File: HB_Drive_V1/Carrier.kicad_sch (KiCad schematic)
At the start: 0 parts

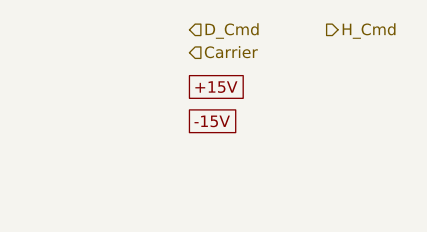
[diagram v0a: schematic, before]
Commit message: fixes git and adds a first revision of the Inner Current Regulator (NOT COMPLETE)
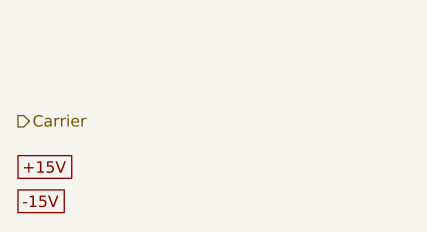
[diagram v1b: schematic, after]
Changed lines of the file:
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@@
 	(generator_version "10.0")
 	(paper "A4")
-	(global_label "-15V"
+	(global_label "+15V"
 		(shape passive)
-		(at 139.7 86.36 0)
+		(at 120.65 91.44 0)
 		(fields_autoplaced yes)
 		(effects
@@
 		)
 		(property "Intersheetrefs" "${INTERSHEET_REFS}"
-			(at 146.6539 86.36 0)
+			(at 127.6039 91.44 0)
 			(hide yes)
 			(show_name no)
@@
 		)
 	)
-	(global_label "+15V"
+	(global_label "-15V"
 		(shape passive)
-		(at 139.7 82.55 0)
+		(at 120.65 95.25 0)
 		(fields_autoplaced yes)
 		(effects
@@
 		)
 		(property "Intersheetrefs" "${INTERSHEET_REFS}"
-			(at 146.6539 82.55 0)
+			(at 127.6039 95.25 0)
 			(hide yes)
 			(show_name no)
@@
 		)
 	)
-	(hierarchical_label "D_Cmd"
-		(shape input)
-		(at 139.7 76.2 0)
+	(hierarchical_label "Carrier"
+		(shape output)
+		(at 120.65 86.36 0)
 		(effects
 			(font
-				(size 1.27 1.27)
-			)
-			(justify left)
-		)
-	)
-	(hierarchical_label "Carrier"
-		(shape input)
-		(at 139.7 78.74 0)
-		(effects
-			(font
-				(size 1.27 1.27)
-			)
-			(justify left)
-		)
-	)
-	(hierarchical_label "H_Cmd"
-		(shape output)
-		(at 154.94 76.2 0)
-		(effects
-			(font

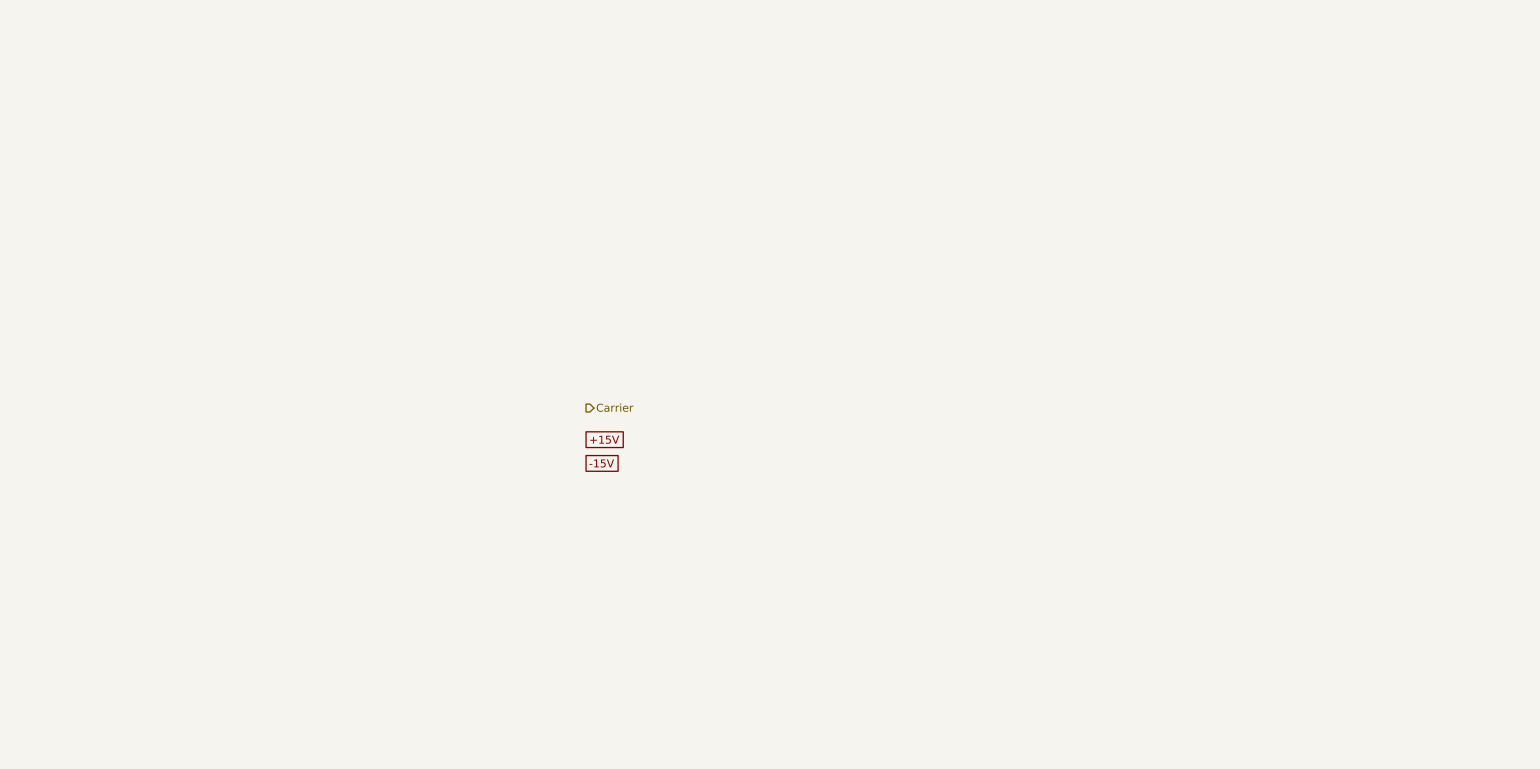
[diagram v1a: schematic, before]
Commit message: Adds Carrier Wave Circuit and Comparator Circuit
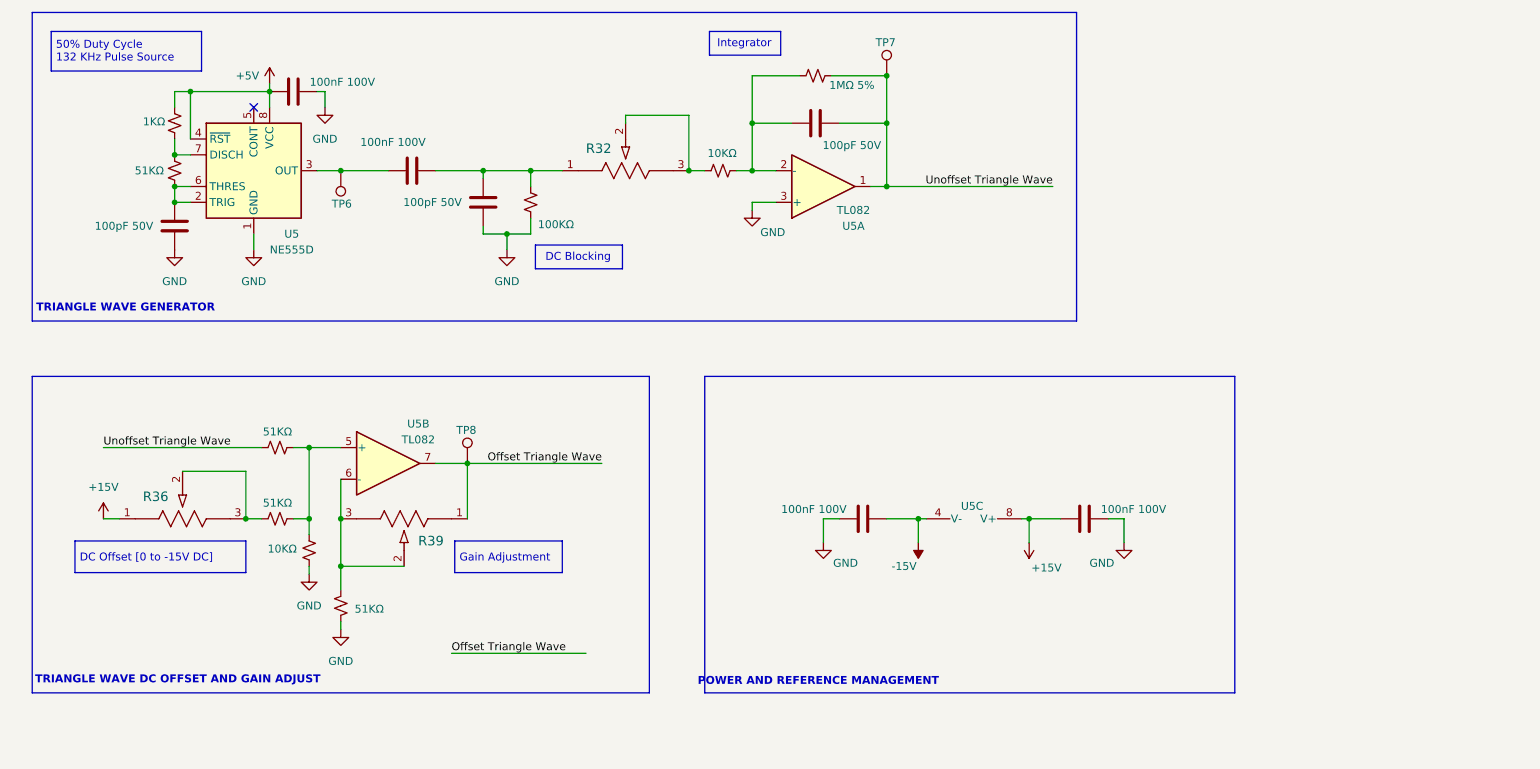
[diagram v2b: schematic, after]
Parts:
- added C15, C6, C9: 100pF 50V, Capacitor_SMD:C_0603_1608Metric, symbol Device:C
- added C16, C19, C5, C7: 100nF 100V, Capacitor_SMD:C_0603_1608Metric, symbol Device:C
- added R29: 1KΩ, Resistor_SMD:R_0603_1608Metric_Pad0.98x0.95mm_HandSolder, symbol Device:R_Small_US
- added R30, R34, R37, R40: 51KΩ, Resistor_SMD:R_0603_1608Metric_Pad0.98x0.95mm_HandSolder, symbol Device:R_Small_US
- added R31: 100KΩ, Resistor_SMD:R_0603_1608Metric_Pad0.98x0.95mm_HandSolder, symbol Device:R_Small_US
- added R32, R36, R39: PV36W104C01B00, PV36W104C01B00:POT_PV36W_BRN, symbol PV36W104C01B00:PV36W104C01B00
- added R33, R38: 10KΩ, Resistor_SMD:R_0603_1608Metric_Pad0.98x0.95mm_HandSolder, symbol Device:R_Small_US
- added R35: 1MΩ 5%, Resistor_SMD:R_0603_1608Metric_Pad0.98x0.95mm_HandSolder, symbol Device:R_Small_US
- added TP6, TP7, TP8: TestPoint, TestPoint:TestPoint_Loop_D2.60mm_Drill1.6mm_Beaded, symbol Connector:TestPoint
- added U5: TL082, Package_SO:SOIC-8_5.3x5.3mm_P1.27mm, symbol Amplifier_Operational:TL082
- added U5: NE555D, Package_SO:SOIC-8_3.9x4.9mm_P1.27mm, symbol Timer:NE555D
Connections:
- net +15V: now also C19.2, R36.1, U5.8 (V+)
- net -15V: now also C16.1, U5.4 (V-)
- new net: R29.2, R30.1, U5.7 (DISCH)
- new net: C6.1, R30.2, U5.2 (TRIG), U5.6 (THRES)
- new net: C15.1, R33.2, R35.1, U5.2 (-)
- new net: R39.2, R39.3, R40.1, U5.6 (-)
- new net: R34.1, R37.1, R38.2, U5.5 (+)
- new net: C7.1, C9.1, R31.1, R32.1
- new net: R32.2, R32.3, R33.1
- new net: R36.2, R36.3, R37.2
- new net: C7.2, TP6.1, U5.3 (OUT)
- new net +5V: C5.2, R29.1, U5.4 (~{RST}), U5.8 (VCC)
- new net GND: C16.2, C19.1, C5.1, C6.2, C9.2, R31.2, R38.1, R40.2, U5.1 (GND), U5.3 (+)
- new net Offset Triangle Wave: R39.1, TP8.1, U5.7
- new net Unoffset Triangle Wave: C15.2, R34.2, R35.2, TP7.1, U5.1
- no-connect marks 0 -> 1
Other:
- note added: "50% Duty Cycle 132 KHz Pulse Source"
- note added: "DC Blocking"
- note added: "DC Offset [0 to -15V DC]"
- note added: "Gain Adjustment"
- note added: "Integrator"
- note added: "POWER AND REFERENCE MANAGEMENT"
- note added: "TRIANGLE WAVE DC OFFSET AND GAIN ADJUST"
- note added: "TRIANGLE WAVE GENERATOR"

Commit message: Notes from conversation PF + MS
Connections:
- net Offset Triangle Wave renamed Carrier
- net Unoffset Triangle Wave renamed Bipolar Triangle Wave
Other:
- moved on the sheet: R36, R39, TP8, U5B

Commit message: adds 10v reference and DC offsets / gain control to I_fdbk and V_fdbk
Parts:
- added C39, C42: 10nF, Capacitor_SMD:C_0603_1608Metric_Pad1.08x0.95mm_HandSolder, symbol Device:C_Small
- added D6, D7: 1N4148W, Diode_SMD:D_SOD-123, symbol Diode:1N4148W
- added R57: 1KΩ, Resistor_SMD:R_0603_1608Metric_Pad0.98x0.95mm_HandSolder, symbol Device:R_Small_US
- added R70: PV36W103C01B00, PV36W104C01B00:POT_PV36W_BRN, symbol PV36W103C01B00:PV36W103C01B00
- added R71: 680Ω, Resistor_SMD:R_0603_1608Metric_Pad0.98x0.95mm_HandSolder, symbol Device:R_Small_US
- added TP9: TestPoint, TestPoint:TestPoint_Loop_D2.60mm_Drill1.6mm_Beaded, symbol Connector:TestPoint
- added U22: NE555D, Package_SO:SOIC-8_3.9x4.9mm_P1.27mm, symbol Timer:NE555D
- renumbered C6 to C18, C5 to C19, C7 to C20, C9 to C21, C15 to C22, C16 to C23, C19 to C24, R36 to R35, R29 to R36, R30 to R37, R34 to R38, R37 to R39, R38 to R40, R40 to R41, R39 to R42, R31 to R43, R32 to R44, R33 to R45, R35 to R46, TP7 to TP10, TP6 to TP7, U5 to U10, U5 to U11
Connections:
- net +5V: now also R57.1, R71.1, U22.4 (~{RST}), U22.8 (VCC)
- net GND: now also C39.2, C42.1, U22.1 (GND)
- net at C20.1, C21.1, R43.1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: now also TP9.1
- new net: C39.1, D6.1 (K), D7.2 (A), R70.1, U22.2 (TRIG), U22.6 (THRES)
- new net: D6.2 (A), R57.2
- new net: R70.2, U22.7 (DISCH)
- new net: R70.3, R71.2
- new net: C42.2, U22.5 (CONT)
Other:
- note added: "???? BONUS WEIRD TIMER THING ????"
- moved on the sheet: R35, R42, R44, TP10, TP7, TP8, U10, U11A, U11B, U11C
